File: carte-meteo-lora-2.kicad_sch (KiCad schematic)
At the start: 72 parts, among them J1 USB_C_Receptacle_USB2.0_14P, J4 Conn_01x04_Pin, J6 Conn_Coaxial, J7 Conn_Coaxial, J8 Conn_Coaxial, SW1 SW_Push, SW2 SW_Push, U3 HS96L03W2C03, U4 LDL212PV33R, U6 ESP32-C5, U8 SX1262TR8-GC, Y1 48M

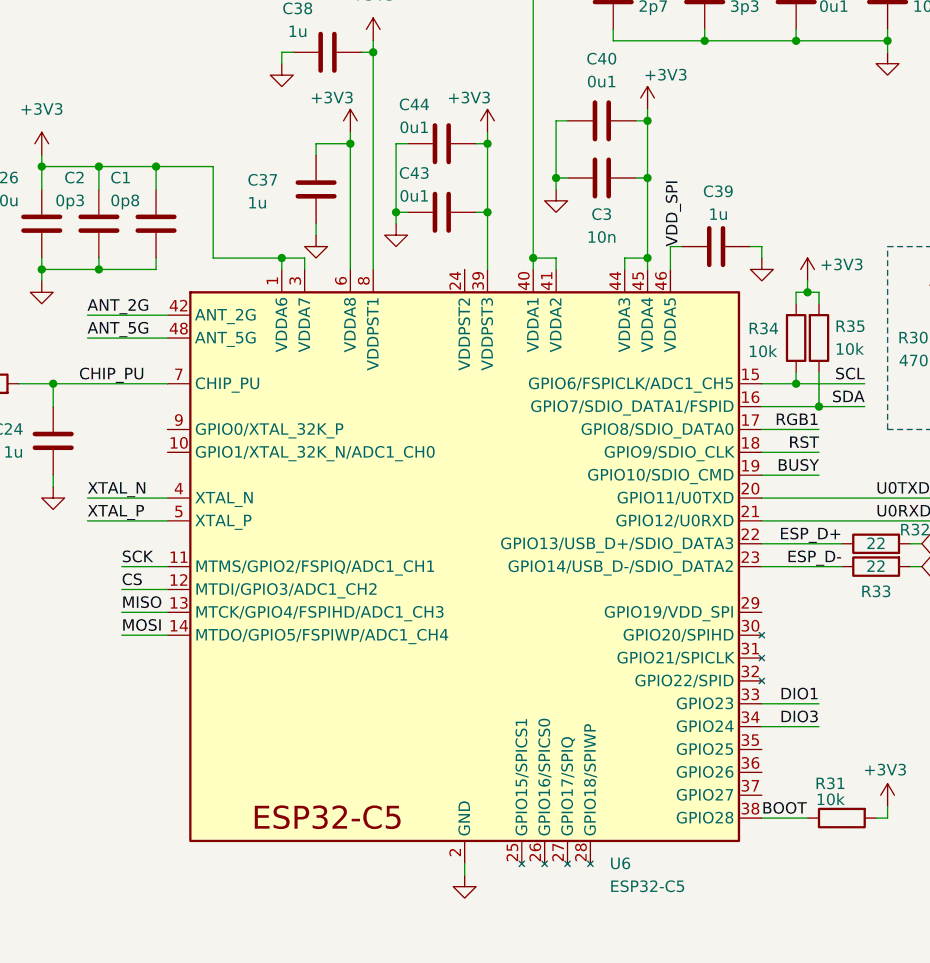
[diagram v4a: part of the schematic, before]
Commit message: schem: add no connects
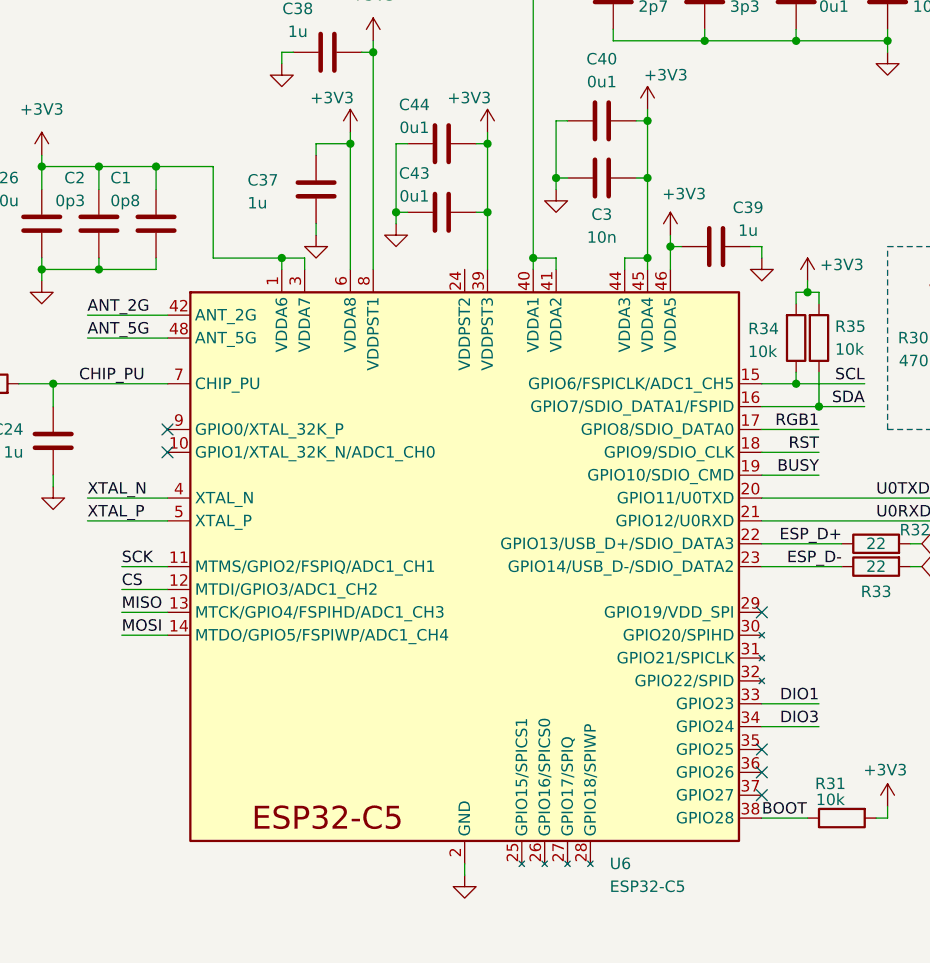
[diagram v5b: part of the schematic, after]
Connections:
- net VDD_SPI is gone; now on net +3V3: C39.1, U6.46 (VDDA5)
- no-connect marks 5 -> 11
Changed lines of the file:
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@@
 	)
 	(junction
+		(at 226.06 58.42)
+		(diameter 0)
+		(color 0 0 0 0)
+	)
+	(junction
 		(at 162.56 60.96)
 		(diameter 0)
@@
 	)
 	(no_connect
+		(at 170.18 81.28)
+	)
+	(no_connect
+		(at 236.22 119.38)
+	)
+	(no_connect
 		(at 114.3 100.33)
 	)
@@
 	)
 	(no_connect
+		(at 236.22 114.3)
+	)
+	(no_connect
 		(at 87.63 130.81)
 	)
@@
 		(at 114.3 130.81)
 	)
+	(no_connect
+		(at 236.22 116.84)
+	)
+	(no_connect
+		(at 170.18 78.74)
+	)
+	(no_connect
+		(at 236.22 99.06)
+	)
 	(wire
 		(pts
@@
 	(wire
 		(pts
+			(xy 226.06 57.15) (xy 226.06 58.42)
+		)
+		(stroke
+			(width 0)
+			(type default)
+		)
+	)
+	(wire
+		(pts
 			(xy 66.04 160.02) (xy 64.77 160.02)
 		)
@@
 		)
 	)
-	(label "VDD_SPI"
-		(at 227.33 58.42 90)
-		(effects
-			(font
-				(size 1.27 1.27)
-			)
-			(justify left bottom)
-		)
-	)
 	(label "SCK"
 		(at 165.1 93.98 0)
@@
 		(dnp no)
 		(property "Reference" "C39"
-			(at 231.394 52.324 90)
+			(at 234.696 54.102 90)
 			(show_name no)
 			(do_not_autoplace no)
@@
 		)
 		(property "Value" "1u"
-			(at 231.394 54.864 90)
+			(at 234.696 56.642 90)
 			(show_name no)
 			(do_not_autoplace no)
@@
 					(unit 1)
 				)
+			)
+		)
+	)
+	(symbol
+		(lib_id "power:+3V3")
+		(at 226.06 57.15 0)
+		(mirror y)
+		(unit 1)
+		(body_style 1)
+		(exclude_from_sim no)
+		(in_bom yes)
+		(on_board yes)
+		(in_pos_files yes)
+		(dnp no)
+		(property "Reference" "#PWR092"
+			(at 226.06 60.96 0)
+			(hide yes)
+			(show_name no)
+			(do_not_autoplace no)
+			(effects
+				(font
+					(size 1.27 1.27)
+				)
+			)
+		)
+		(property "Value" "+3V3"
+			(at 227.584 52.578 0)
+			(show_name no)
+			(do_not_autoplace no)
+			(effects
+				(font
+					(size 1.27 1.27)
+				)
+			)
+		)
+		(property "Footprint" ""
+			(at 226.06 57.15 0)
+			(hide yes)
+			(show_name no)
+			(do_not_autoplace no)
+			(effects
+				(font
+					(size 1.27 1.27)
+				)
+			)
+		)
+		(property "Datasheet" ""
+			(at 226.06 57.15 0)
+			(hide yes)
+			(show_name no)
+			(do_not_autoplace no)
+			(effects
+				(font
+					(size 1.27 1.27)
+				)
+			)
+		)
+		(property "Description" "Power symbol creates a global label with name \"+3V3\""
+			(at 226.06 57.15 0)
+			(hide yes)
+			(show_name no)
+			(do_not_autoplace no)
+			(effects
+				(font
+					(size 1.27 1.27)
+				)
+			)
+		)
+		(pin "1"
+		)
+		(instances
+			(project "carte-meteo-lora-2"
+				(path "/14cd50fe-ec77-4829-bd74-9322c036cdc1"
+					(reference "#PWR092")
+					(unit 1)
+				)

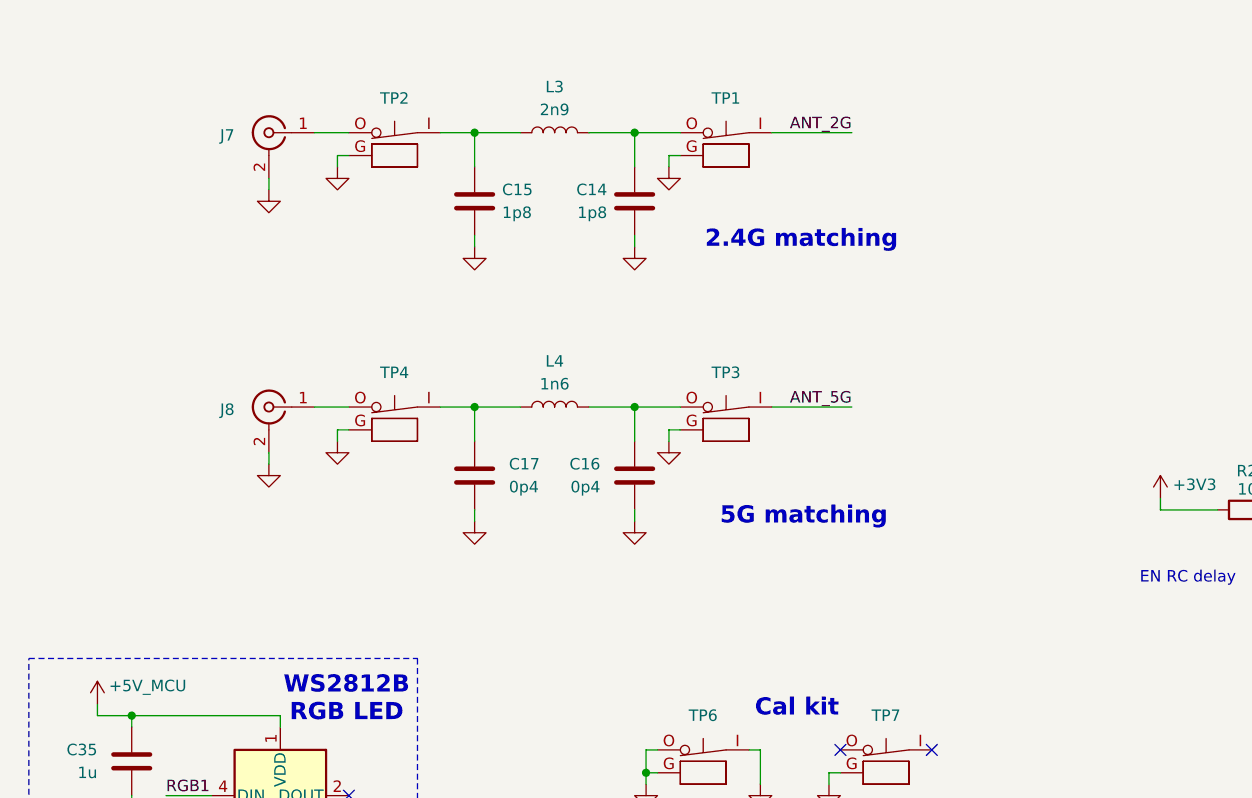
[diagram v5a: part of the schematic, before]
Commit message: schem: add led pwr indicators
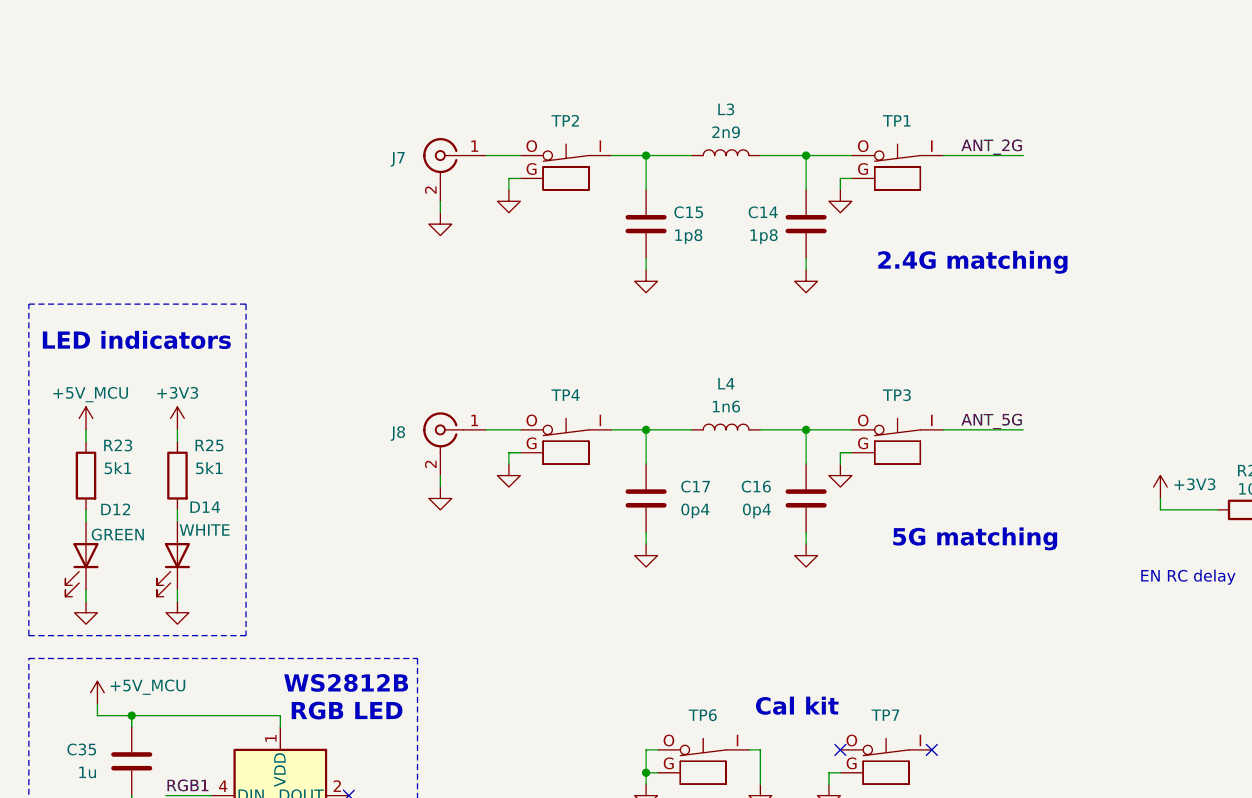
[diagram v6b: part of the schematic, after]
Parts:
- added D12: GREEN, LED_SMD:LED_0805_2012Metric, symbol Device:LED
- added D14: WHITE, LED_SMD:LED_0603_1608Metric, symbol Device:LED
- added R23, R25: 5k1, Resistor_SMD:R_0402_1005Metric, symbol Device:R
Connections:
- net +3V3: now also R25.1
- net +5V_MCU: now also R23.1
- net GND: now also D12.1 (K), D14.1 (K)
- new net: D14.2 (A), R25.2
- new net: D12.2 (A), R23.2
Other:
- note added: "LED indicators"
- moved on the sheet: C14, C15, C16, C17, J7, J8, L3, L4, TP1, TP2, TP3, TP4

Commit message: schem: add test points
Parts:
- added TP17, TP18, TP19, TP20: TestPoint, TestPoint:TestPoint_Pad_D1.0mm, symbol Connector:TestPoint
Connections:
- net CS: now also TP18.1
- net MISO: now also TP19.1
- net MOSI: now also TP20.1
- net SCK: now also TP17.1

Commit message: schem: add net classes
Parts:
- U3: footprint Pers:HS96L03W2C03 -> GLCS:HS96L03W2C03
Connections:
- net +3V3: now also U6.24 (VDDPST2)
- net RF_LR: now reaches J6.1 (In), U8.21 (ANT)
- net RF_TRANS_5G: now reaches C17.2, L4.2, TP4.I
- net RF_ESP_5G: now reaches C16.2, L4.1, TP3.O
- net RF_ESP_2G: now reaches C14.1, L3.1, TP1.O
- net RF_TRANS_2G: now reaches C15.1, L3.2, TP2.I
- net RF_CN_5G: now reaches J8.1 (In), TP4.O
- net RF_CN_2G: now reaches J7.1 (In), TP2.O
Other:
- moved on the sheet: J7, J8
